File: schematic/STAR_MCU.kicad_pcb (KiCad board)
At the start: 2 copper layers, 114 parts, among them J11 6120XX21621_61200621621, J13 6120XX21621_61200821621, J14 6120XX21621_61200821621, J15 6120XX21621_61200821621, J16 6120XX21621_61200821621, J18 6120XX21621_61200621621, J19 6120XX21621_61200821621, J2 USB4216-03-A, J20 S5B-XH-A, J21 6120XX21621_61200621621, J4 E1E2-Emulator-Interface, J7 USB4216-03-A, J8 Conn_02x20_Odd_Even, U1 R5F572NNHGFP-30, U2 CY7C65213A-28PVXI, U3 TVS2200DRV, U4 LDL1117S33R, U5 TPS2116DRLR, U6 TVS2200DRV

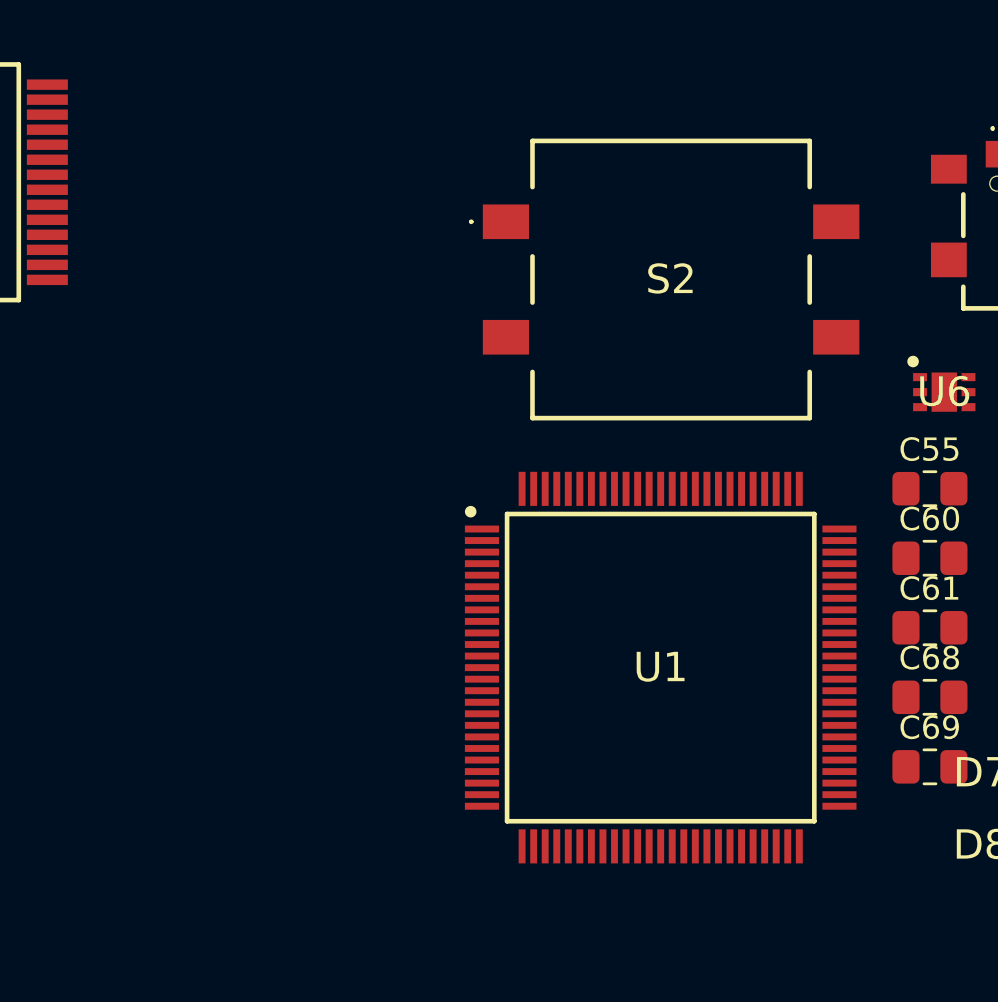
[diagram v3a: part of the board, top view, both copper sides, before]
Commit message: reorganize PMOD connectors and add status LEDs
- PMOD JA: reorder pins 7-10 (DC, RST, GPIO, CS1) for standard display compatibility
- PMOD JB: change from I2C to 6-pin GPIO (PC6, P55, P54, PA2)
- PMOD JC: change from UART to 6-pin I2C with interrupts (PC4, PC5, PC2, PC3)
- PMOD JD: add new 6-pin GPIO expansion (PD7, PD6, PD5, PD4)
- Add ERROR_STATUS_LED (PB1) and SYSTEM_HEARTBEAT_LED (PB0)
- Add SAMTEC SSW-106-02-G-D-RA and SSW-106-02-G-S-RA connector libraries
- Update schematic labels, documentation tables, and netclass colors
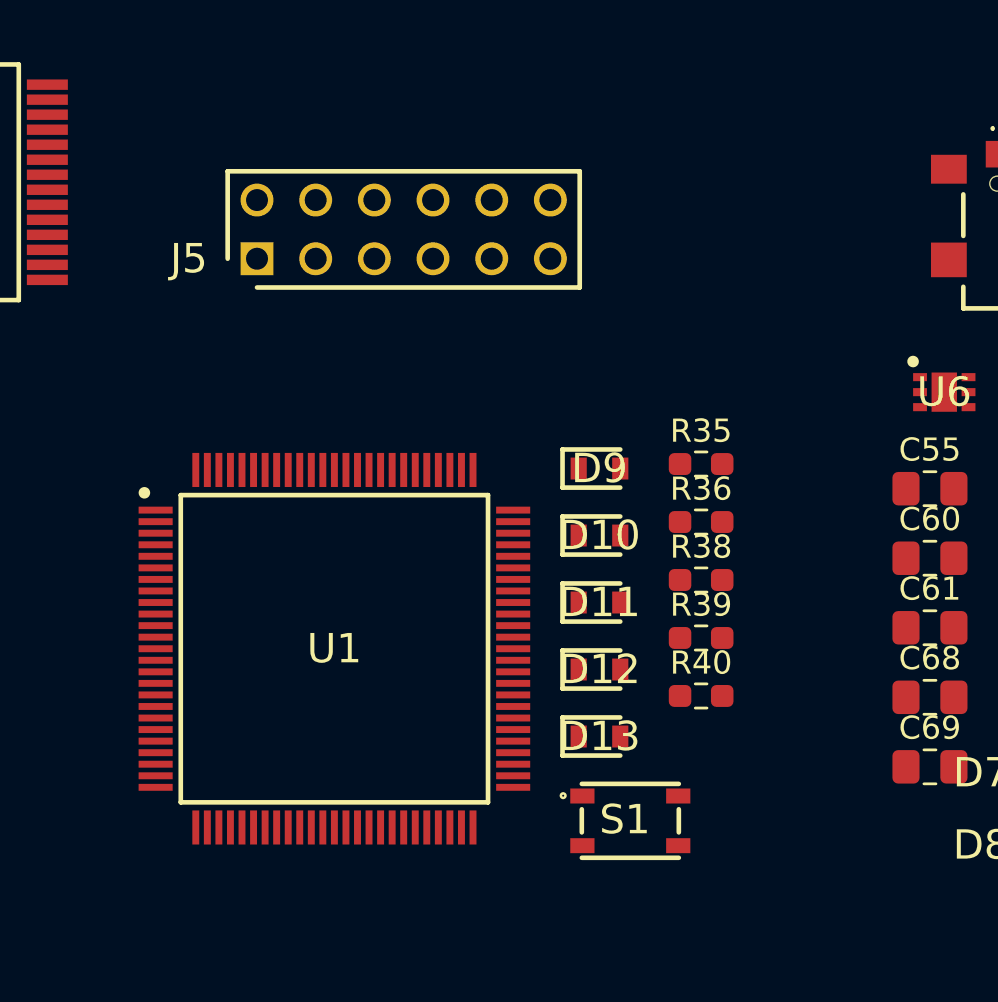
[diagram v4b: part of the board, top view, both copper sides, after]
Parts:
- removed S2: PTS125SM73SMTR21M_LFS, PTS125SM73SMTR21M_LFS:PTS125SM73SMTR21MLFS
- added D10: RED, SML-D12Y1WT86:LEDC1608X55N, F.Cu at (194.2, 119.0)
- added D11: RED, SML-D12Y1WT86:LEDC1608X55N, F.Cu at (194.2, 121.9)
- added D12: RED, SML-D12Y1WT86:LEDC1608X55N, F.Cu at (194.2, 124.8)
- added D13: RED, SML-D12Y1WT86:LEDC1608X55N, F.Cu at (194.2, 127.7)
- added D9: RED, SML-D12Y1WT86:LEDC1608X55N, F.Cu at (194.2, 116.1)
- added J5: 5-534998-6, 5-534998-6:RHDR12W77P254_2X6_1524X503X673P, F.Cu at (179.4, 107.0)
- added R35: 68R, Resistor_SMD:R_0603_1608Metric_Pad0.98x0.95mm_HandSolder, F.Cu at (198.6, 115.9)
- added R36: 68R, Resistor_SMD:R_0603_1608Metric_Pad0.98x0.95mm_HandSolder, F.Cu at (198.6, 118.4)
- added R38: 68R, Resistor_SMD:R_0603_1608Metric_Pad0.98x0.95mm_HandSolder, F.Cu at (198.6, 120.9)
- added R39: 68R, Resistor_SMD:R_0603_1608Metric_Pad0.98x0.95mm_HandSolder, F.Cu at (198.6, 123.4)
- added R40: 68R, Resistor_SMD:R_0603_1608Metric_Pad0.98x0.95mm_HandSolder, F.Cu at (198.6, 125.9)
- added S1: RST, SKRPACE010:SMT_4.2X3.2_, F.Cu at (195.5, 131.4)
- moved U1 14.1 mm to (182.7, 123.9)
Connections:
- net /JA2_NMIn renamed /JP_UPSEL
- net /MOTOR_DRIVER_ENCODER4_OUTPUT_A renamed /ENCODER3_PHASE_A
- net /MOTOR_DRIVER_ENCODER4_OUTPUT_B renamed /ENCODER3_PHASE_B
- net /MOTOR_DRIVER_MOTOR4_EN_IN1 renamed /MOTOR3_EN
- net /MOTOR_DRIVER_MOTOR4_IPROPI renamed /MOTOR3_IPROPI
- net /MOTOR_DRIVER_MOTOR4_PH_IN2 renamed /MOTOR3_PH
- net /MOTOR_DRIVER_MOTOR4_nFAULT renamed /MOTOR3_nFAULT
- net /MOTOR_DRIVER_P3V3 renamed /P3V3_BUCK
- J13 pad 1: /MOTOR_DRIVER_SPI2_MOTOR1_nCS -> /RSPIC_MOTOR0_nCS
- J13 pad 2: /MOTOR_DRIVER_SPI2_CM_COPI -> /RSPIC_COPI
- J13 pad 3: /MOTOR_DRIVER_SPI2_MOTOR2_nCS -> /RSPIC_MOTOR1_nCS
- J13 pad 4: /MOTOR_DRIVER_SPI2_CM_SCLK -> /RSPIC_SCLK
- J13 pad 5: /MOTOR_DRIVER_SPI2_MOTOR3_nCS -> /RSPIC_MOTOR2_nCS
- J13 pad 6: /MOTOR_DRIVER_SPI2_CM_CIPO -> /RSPIC_CIPO
- J13 pad 7: /MOTOR_DRIVER_SPI2_MOTOR4_nCS -> /RSPIC_MOTOR3_nCS
- J14 pad 1: /MOTOR_DRIVER_ENCODER1_OUTPUT_A -> /ENCODER0_PHASE_A
- J14 pad 2: /MOTOR_DRIVER_ENCODER1_OUTPUT_B -> /ENCODER0_PHASE_B
- J14 pad 3: /MOTOR_DRIVER_ENCODER2_OUTPUT_A -> /ENCODER1_PHASE_A
- J14 pad 4: /MOTOR_DRIVER_ENCODER2_OUTPUT_B -> /ENCODER1_PHASE_B
- J14 pad 5: /MOTOR_DRIVER_ENCODER3_OUTPUT_A -> /ENCODER2_PHASE_A
- J14 pad 6: /MOTOR_DRIVER_ENCODER3_OUTPUT_B -> /ENCODER2_PHASE_B
- J15 pad 1: /MOTOR_DRIVER_MOTOR1_nFAULT -> /MOTOR0_nFAULT
- J15 pad 2: /MOTOR_DRIVER_MOTOR1_IPROPI -> /MOTOR0_IPROPI
- J15 pad 3: /MOTOR_DRIVER_MOTOR2_nFAULT -> /MOTOR1_nFAULT
- J15 pad 4: /MOTOR_DRIVER_MOTOR2_IPROPI -> /MOTOR1_IPROPI
- J15 pad 5: /MOTOR_DRIVER_MOTOR3_nFAULT -> /MOTOR2_nFAULT
- J15 pad 6: /MOTOR_DRIVER_MOTOR3_IPROPI -> /MOTOR2_IPROPI
- J16 pad 1: /MOTOR_DRIVER_MOTOR1_EN_IN1 -> /MOTOR0_EN
- J16 pad 2: /MOTOR_DRIVER_MOTOR1_PH_IN2 -> /MOTOR0_PH
- J16 pad 3: /MOTOR_DRIVER_MOTOR2_EN_IN1 -> /MOTOR1_EN
- J16 pad 4: /MOTOR_DRIVER_MOTOR2_PH_IN2 -> /MOTOR1_PH
- J16 pad 5: /MOTOR_DRIVER_MOTOR3_EN_IN1 -> /MOTOR2_EN
- J16 pad 6: /MOTOR_DRIVER_MOTOR3_PH_IN2 -> /MOTOR2_PH
- J4 pad 13: /EMU_RESn -> /DBG_RESETn
- J8 pad 19: /ESP_PI_SPI3_PM_COPI -> /RPI5_RSPIA_COPI
- J8 pad 21: /ESP_PI_SPI3_PM_CIPO -> /RPI5_RSPIA_CIPO
- J8 pad 23: /ESP_PI_SPI3_PM_SCLK -> /RPI5_RSPIA_SCLK
- J8 pad 24: /ESP_PI_SPI3_PM_CS -> /RPI5_RSPIA_CS
- J8 pad 38: /ESP_PI_SPI3_PM_DRDY1 -> unconnected-(J8-Pin_38-Pad38)
- J8 pad 40: /ESP_PI_SPI3_PM_DRDY2 -> unconnected-(J8-Pin_40-Pad40)
- R21 pad 1: Net-(U2-RESET#) -> /DBG_RESETn
- U1 pad 10: /EMU_RESn -> /DBG_RESETn
- U1 pad 100: unconnected-(U1-P05-Pad100) -> Net-(U1-P05)
- U1 pad 17: unconnected-(U1-P33-Pad17) -> /DBG_RESETn
- U1 pad 18: unconnected-(U1-P32-Pad18) -> /RSPIC_MOTOR2_nCS
- U1 pad 23: unconnected-(U1-P25-Pad23) -> /ENCODER2_PHASE_A
- U1 pad 24: unconnected-(U1-P24-Pad24) -> /ENCODER0_PHASE_A
- U1 pad 25: unconnected-(U1-P23-Pad25) -> /RSPIC_MOTOR1_nCS
- U1 pad 26: unconnected-(U1-P22-Pad26) -> /ENCODER0_PHASE_B
- U1 pad 27: unconnected-(U1-P21-Pad27) -> /CHARGER_I2C_CLOCK
- U1 pad 28: unconnected-(U1-P20-Pad28) -> /CHARGER_I2C_DATA
- U1 pad 29: unconnected-(U1-P17-Pad29) -> /RSPIC_MOTOR0_nCS
- U1 pad 31: unconnected-(U1-P15/RXD1-Pad31) -> /ENCODER0_PHASE_B
- U1 pad 32: unconnected-(U1-P14-Pad32) -> /ENCODER0_PHASE_A
- U1 pad 33: unconnected-(U1-P13/TXD2-Pad33) -> /BMS_SMBUS_CLK
- U1 pad 34: unconnected-(U1-P12/RXD2-Pad34) -> /BMS_SMBUS_DATA
- U1 pad 39: unconnected-(U1-P55-Pad39) -> /PMOD_JB_GPIO1
- U1 pad 4: unconnected-(U1-PJ3-Pad4) -> Net-(U1-PJ3)
- U1 pad 40: unconnected-(U1-P54-Pad40) -> /PMOD_JB_GPIO2
- U1 pad 41: unconnected-(U1-P53-Pad41) -> /PMOD_JA_SCK
- U1 pad 42: unconnected-(U1-P52-Pad42) -> /PMOD_JA_CS0
- U1 pad 43: unconnected-(U1-P51-Pad43) -> /PMOD_JA_CIPO
- U1 pad 44: unconnected-(U1-P50-Pad44) -> /PMOD_JA_COPI
- U1 pad 46: unconnected-(U1-PC6-Pad46) -> /PMOD_JB_GPIO0
- U1 pad 47: unconnected-(U1-PC5-Pad47) -> /PMOD_JB_INT2
- U1 pad 48: unconnected-(U1-PC4-Pad48) -> /PMOD_JB_INT1
- U1 pad 49: unconnected-(U1-PC3-Pad49) -> /PMOD_JB_SDA
- U1 pad 50: unconnected-(U1-PC2-Pad50) -> /PMOD_JB_SCL
- U1 pad 51: unconnected-(U1-PC1-Pad51) -> /ENCODER1_PHASE_A
- U1 pad 52: unconnected-(U1-PC0-Pad52) -> /ENCODER1_PHASE_B
- U1 pad 55: unconnected-(U1-PB5-Pad55) -> /PMOD_JA_CS1
- U1 pad 56: unconnected-(U1-PB4-Pad56) -> /PMOD_JA_DC
- U1 pad 57: unconnected-(U1-PB3-Pad57) -> /PMOD_JA_RST
- U1 pad 58: unconnected-(U1-PB2-Pad58) -> /PMOD_JA_GPIO
- U1 pad 59: unconnected-(U1-PB1-Pad59) -> /PMOD_JC_GPIO2
- U1 pad 61: unconnected-(U1-PB0-Pad61) -> /PMOD_JC_GPIO3
- U1 pad 63: unconnected-(U1-PA7-Pad63) -> /RPI5_RSPIA_CIPO
- U1 pad 64: unconnected-(U1-PA6-Pad64) -> /RPI5_RSPIA_COPI
- U1 pad 65: unconnected-(U1-PA5-Pad65) -> /RPI5_RSPIA_SCLK
- U1 pad 66: unconnected-(U1-PA4-Pad66) -> /RPI5_RSPIA_CS
- U1 pad 67: unconnected-(U1-PA3-Pad67) -> /ENCODER2_PHASE_B
- U1 pad 68: unconnected-(U1-PA2-Pad68) -> /PMOD_JB_GPIO3
- U1 pad 69: unconnected-(U1-PA1-Pad69) -> Net-(U1-PA1)
- U1 pad 70: unconnected-(U1-PA0-Pad70) -> /RSPIC_MOTOR3_nCS
- U1 pad 71: unconnected-(U1-PE7-Pad71) -> /MOTOR2_PH
- U1 pad 72: unconnected-(U1-PE6-Pad72) -> /MOTOR2_EN
- U1 pad 73: unconnected-(U1-PE5-Pad73) -> /MOTOR0_PH
- U1 pad 74: unconnected-(U1-PE4-Pad74) -> /MOTOR0_PH
- U1 pad 75: unconnected-(U1-PE3-Pad75) -> /MOTOR1_PH
- U1 pad 76: unconnected-(U1-PE2-Pad76) -> /MOTOR0_EN
- U1 pad 77: unconnected-(U1-PE1-Pad77) -> /MOTOR0_EN
- U1 pad 78: unconnected-(U1-PE0-Pad78) -> /MOTOR1_EN
- U1 pad 79: unconnected-(U1-PD7-Pad79) -> /PMOD_JC_UART_TX
- U1 pad 80: unconnected-(U1-PD6-Pad80) -> /PMOD_JC_UART_RX
- U1 pad 81: unconnected-(U1-PD5-Pad81) -> /PMOD_JC_RTS
- U1 pad 82: unconnected-(U1-PD4-Pad82) -> /PMOD_JC_CTS
- U1 pad 83: unconnected-(U1-PD3-Pad83) -> /RSPIC_SCLK
- U1 pad 84: unconnected-(U1-PD2-Pad84) -> /RSPIC_CIPO
- U1 pad 85: unconnected-(U1-PD1-Pad85) -> /RSPIC_COPI
- U1 pad 86: unconnected-(U1-PD0-Pad86) -> Net-(U1-PD0)
- U1 pad 87: unconnected-(U1-P47-Pad87) -> /MOTOR2_nFAULT
- U1 pad 88: unconnected-(U1-P46-Pad88) -> /MOTOR1_nFAULT
- U1 pad 89: unconnected-(U1-P45-Pad89) -> /MOTOR0_nFAULT
- U1 pad 90: unconnected-(U1-P44-Pad90) -> /MOTOR0_nFAULT
- U1 pad 91: unconnected-(U1-P43-Pad91) -> /MOTOR2_IPROPI
- U1 pad 92: unconnected-(U1-P42-Pad92) -> /MOTOR1_IPROPI
- U1 pad 93: unconnected-(U1-P41-Pad93) -> /MOTOR0_IPROPI
- U1 pad 95: unconnected-(U1-P40-Pad95) -> /MOTOR0_IPROPI
- U1 pad 98: unconnected-(U1-P07-Pad98) -> Net-(U1-P07)
- U2 pad 19: Net-(U2-RESET#) -> /DBG_RESETn

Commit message: MCU is ready for review
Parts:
- added D14: RED, SML-D12Y1WT86:LEDC1608X55N, F.Cu at (66.6, 90.2)
- added D15: RED, SML-D12Y1WT86:LEDC1608X55N, F.Cu at (66.6, 93.1)
- added D16: RED, SML-D12Y1WT86:LEDC1608X55N, F.Cu at (66.6, 96.0)
- added D17: RED, SML-D12Y1WT86:LEDC1608X55N, F.Cu at (66.6, 98.9)
- added D18: RED, SML-D12Y1WT86:LEDC1608X55N, F.Cu at (66.6, 101.8)
- added D19: RED, SML-D12Y1WT86:LEDC1608X55N, F.Cu at (71.0, 90.2)
- added D20: RED, SML-D12Y1WT86:LEDC1608X55N, F.Cu at (71.0, 93.1)
- added D21: RED, SML-D12Y1WT86:LEDC1608X55N, F.Cu at (71.0, 96.0)
- added D22: RED, SML-D12Y1WT86:LEDC1608X55N, F.Cu at (71.0, 98.9)
- added D23: RED, SML-D12Y1WT86:LEDC1608X55N, F.Cu at (71.0, 101.8)
- added D24: RED, SML-D12Y1WT86:LEDC1608X55N, F.Cu at (75.5, 90.2)
- added D25: RED, SML-D12Y1WT86:LEDC1608X55N, F.Cu at (75.5, 93.1)
- added D26: RED, SML-D12Y1WT86:LEDC1608X55N, F.Cu at (75.5, 96.0)
- added D27: RED, SML-D12Y1WT86:LEDC1608X55N, F.Cu at (75.5, 98.9)
- added D28: RED, SML-D12Y1WT86:LEDC1608X55N, F.Cu at (75.5, 101.8)
- added J17: SSW-106-02-G-S-RA, SSW-106-02-G-S-RA:SSW-106-XX-YYY-S-RA, F.Cu at (44.0, 52.4)
- added J22: SSW-106-02-G-S-RA, SSW-106-02-G-S-RA:SSW-106-XX-YYY-S-RA, F.Cu at (44.0, 66.7)
- added J23: Conn_02x20_Odd_Even, Connector_PinHeader_2.54mm:PinHeader_2x20_P2.54mm_Vertical, F.Cu at (62.2, 38.2)
- added J24: HC-SR04, Connector_PinSocket_2.54mm:PinSocket_1x04_P2.54mm_Vertical, F.Cu at (69.4, 58.3)
- added J25: HC-SR04, Connector_PinSocket_2.54mm:PinSocket_1x04_P2.54mm_Vertical, F.Cu at (74.0, 58.3)
- added J26: HC-SR04, Connector_PinSocket_2.54mm:PinSocket_1x04_P2.54mm_Vertical, F.Cu at (78.6, 58.3)
- added J27: HC-SR04, Connector_PinSocket_2.54mm:PinSocket_1x04_P2.54mm_Vertical, F.Cu at (83.2, 58.3)
- added J28: Conn_01x02, Connector_PinHeader_2.54mm:PinHeader_1x02_P2.54mm_Vertical, F.Cu at (80.0, 97.6)
- added J31: SSW-106-02-G-S-RA, SSW-106-02-G-S-RA:SSW-106-XX-YYY-S-RA, F.Cu at (44.0, 81.0)
- added J32: SSW-106-02-G-S-RA, SSW-106-02-G-S-RA:SSW-106-XX-YYY-S-RA, F.Cu at (44.0, 95.3)
- added J6: SSW-106-02-G-D-RA, SSW-106-02-G-D-RA:SSW10602GDRA, F.Cu at (82.6, 82.3)
- added R41: 68R, Resistor_SMD:R_0603_1608Metric_Pad0.98x0.95mm_HandSolder, F.Cu at (69.2, 49.7)
- added R42: 68R, Resistor_SMD:R_0603_1608Metric_Pad0.98x0.95mm_HandSolder, F.Cu at (69.2, 52.2)
- added R43: 10k, Resistor_SMD:R_0603_1608Metric_Pad0.98x0.95mm_HandSolder, F.Cu at (69.2, 54.7)
- added R44: 68R, Resistor_SMD:R_0603_1608Metric_Pad0.98x0.95mm_HandSolder, F.Cu at (73.6, 37.1)
- added R45: 68R, Resistor_SMD:R_0603_1608Metric_Pad0.98x0.95mm_HandSolder, F.Cu at (73.6, 39.6)
- added R46: 68R, Resistor_SMD:R_0603_1608Metric_Pad0.98x0.95mm_HandSolder, F.Cu at (73.6, 42.1)
- added R47: 68R, Resistor_SMD:R_0603_1608Metric_Pad0.98x0.95mm_HandSolder, F.Cu at (73.6, 44.6)
- added R48: 68R, Resistor_SMD:R_0603_1608Metric_Pad0.98x0.95mm_HandSolder, F.Cu at (73.6, 47.1)
- added R49: 68R, Resistor_SMD:R_0603_1608Metric_Pad0.98x0.95mm_HandSolder, F.Cu at (73.6, 49.7)
- added R50: 68R, Resistor_SMD:R_0603_1608Metric_Pad0.98x0.95mm_HandSolder, F.Cu at (73.6, 52.2)
- added R51: 68R, Resistor_SMD:R_0603_1608Metric_Pad0.98x0.95mm_HandSolder, F.Cu at (73.6, 54.7)
- added R52: 68R, Resistor_SMD:R_0603_1608Metric_Pad0.98x0.95mm_HandSolder, F.Cu at (77.9, 37.1)
- added R53: 68R, Resistor_SMD:R_0603_1608Metric_Pad0.98x0.95mm_HandSolder, F.Cu at (77.9, 39.6)
- added R54: 68R, Resistor_SMD:R_0603_1608Metric_Pad0.98x0.95mm_HandSolder, F.Cu at (77.9, 42.1)
- added R55: 68R, Resistor_SMD:R_0603_1608Metric_Pad0.98x0.95mm_HandSolder, F.Cu at (77.9, 44.6)
- added R56: 68R, Resistor_SMD:R_0603_1608Metric_Pad0.98x0.95mm_HandSolder, F.Cu at (77.9, 47.1)
- added U7: DS18B20+, DS18B20+:DS18B20, F.Cu at (81.6, 92.6)
- J5: value 5-534998-6 -> SSW-106-02-G-S-RA; footprint 5-534998-6:RHDR12W77P254_2X6_1524X503X673P -> SSW-106-02-G-S-RA:SSW-106-XX-YYY-S-RA
- moved J5 151.9 mm to (44.0, 38.1)
- moved R35 151.5 mm to (69.2, 37.1)
- moved R36 151.5 mm to (69.2, 39.6)
- moved R38 151.5 mm to (69.2, 42.1)
- moved R39 151.5 mm to (69.2, 44.6)
- moved R40 151.5 mm to (69.2, 47.1)
- moved D11 134.6 mm to (62.1, 96.0)
- moved D12 134.6 mm to (62.1, 98.9)
- moved D9 134.6 mm to (62.1, 90.2)
- moved D10 134.6 mm to (62.1, 93.1)
- moved D13 134.6 mm to (62.1, 101.8)
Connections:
- J5 pad 1: unconnected-(J5-Pad1) -> /PMOD_JC_INT1
- J5 pad 2: unconnected-(J5-Pad2) -> /PMOD_JC_INT2
- J5 pad 3: unconnected-(J5-Pad3) -> /PMOD_JC_SCL
- J5 pad 4: unconnected-(J5-Pad4) -> /PMOD_JC_SDA
- J5 pad 5: unconnected-(J5-Pad5) -> GND
- J5 pad 6: unconnected-(J5-Pad6) -> /BOARD_3V3
- J8 pad 1: unconnected-(J8-Pin_1-Pad1) -> /PI_INTERNAL_3V3
- J8 pad 17: unconnected-(J8-Pin_17-Pad17) -> /PI_INTERNAL_3V3
- J8 pad 2: unconnected-(J8-Pin_2-Pad2) -> /PI_INTERNAL_5V0
- J8 pad 4: unconnected-(J8-Pin_4-Pad4) -> /PI_INTERNAL_5V0
- R35 pad 1: Net-(U1-P05) -> /PMOD_JC_INT1
- R36 pad 1: Net-(U1-P07) -> /PMOD_JC_INT2
- R38 pad 1: Net-(U1-PD0) -> /PMOD_JC_SCL
- R39 pad 1: Net-(U1-PA1) -> /PMOD_JC_SDA
- R40 pad 1: Net-(U1-PJ3) -> /PMOD_JF_GPIO0
- U1 pad 100: Net-(U1-P05) -> /PMOD_JF_GPIO0
- U1 pad 27: /CHARGER_I2C_CLOCK -> /PMOD_JF_SCL
- U1 pad 28: /CHARGER_I2C_DATA -> /PMOD_JF_SDA
- U1 pad 4: Net-(U1-PJ3) -> /PMOD_JE_GPIO3
- U1 pad 47: /PMOD_JB_INT2 -> /PMOD_JC_INT2
- U1 pad 48: /PMOD_JB_INT1 -> /PMOD_JC_INT1
- U1 pad 49: /PMOD_JB_SDA -> /PMOD_JC_SDA
- U1 pad 50: /PMOD_JB_SCL -> /PMOD_JC_SCL
- U1 pad 59: /PMOD_JC_GPIO2 -> /PMOD_JE_GPIO2
- U1 pad 61: /PMOD_JC_GPIO3 -> /DS18B20_DQ
- U1 pad 69: Net-(U1-PA1) -> /PMOD_JF_GPIO1
- U1 pad 79: /PMOD_JC_UART_TX -> /PMOD_JD_GPIO0
- U1 pad 80: /PMOD_JC_UART_RX -> /PMOD_JD_GPIO1
- U1 pad 81: /PMOD_JC_RTS -> /PMOD_JD_GPIO2
- U1 pad 82: /PMOD_JC_CTS -> /PMOD_JD_GPIO3
- U1 pad 86: Net-(U1-PD0) -> /PMOD_JE_GPIO1
- U1 pad 98: Net-(U1-P07) -> /PMOD_JE_GPIO0
